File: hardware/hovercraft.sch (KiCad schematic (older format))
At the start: 40 parts, among them J1 USB_OTG, J10 CONN_01X02, J11 CONN_01X02, J12 CONN_01X02, J2 CONN_01X03, J3 CONN_01X03, J4 CONN_01X03, J5 CONN_01X03, J6 CONN_01X03, J7 CONN_01X03, J8 CONN_01X02, J9 CONN_01X02, SW1 RESET, SW2 BOOT, U1 HC-12, U2 ATMEGA32U2-AU, Y1 Crystal_GND24

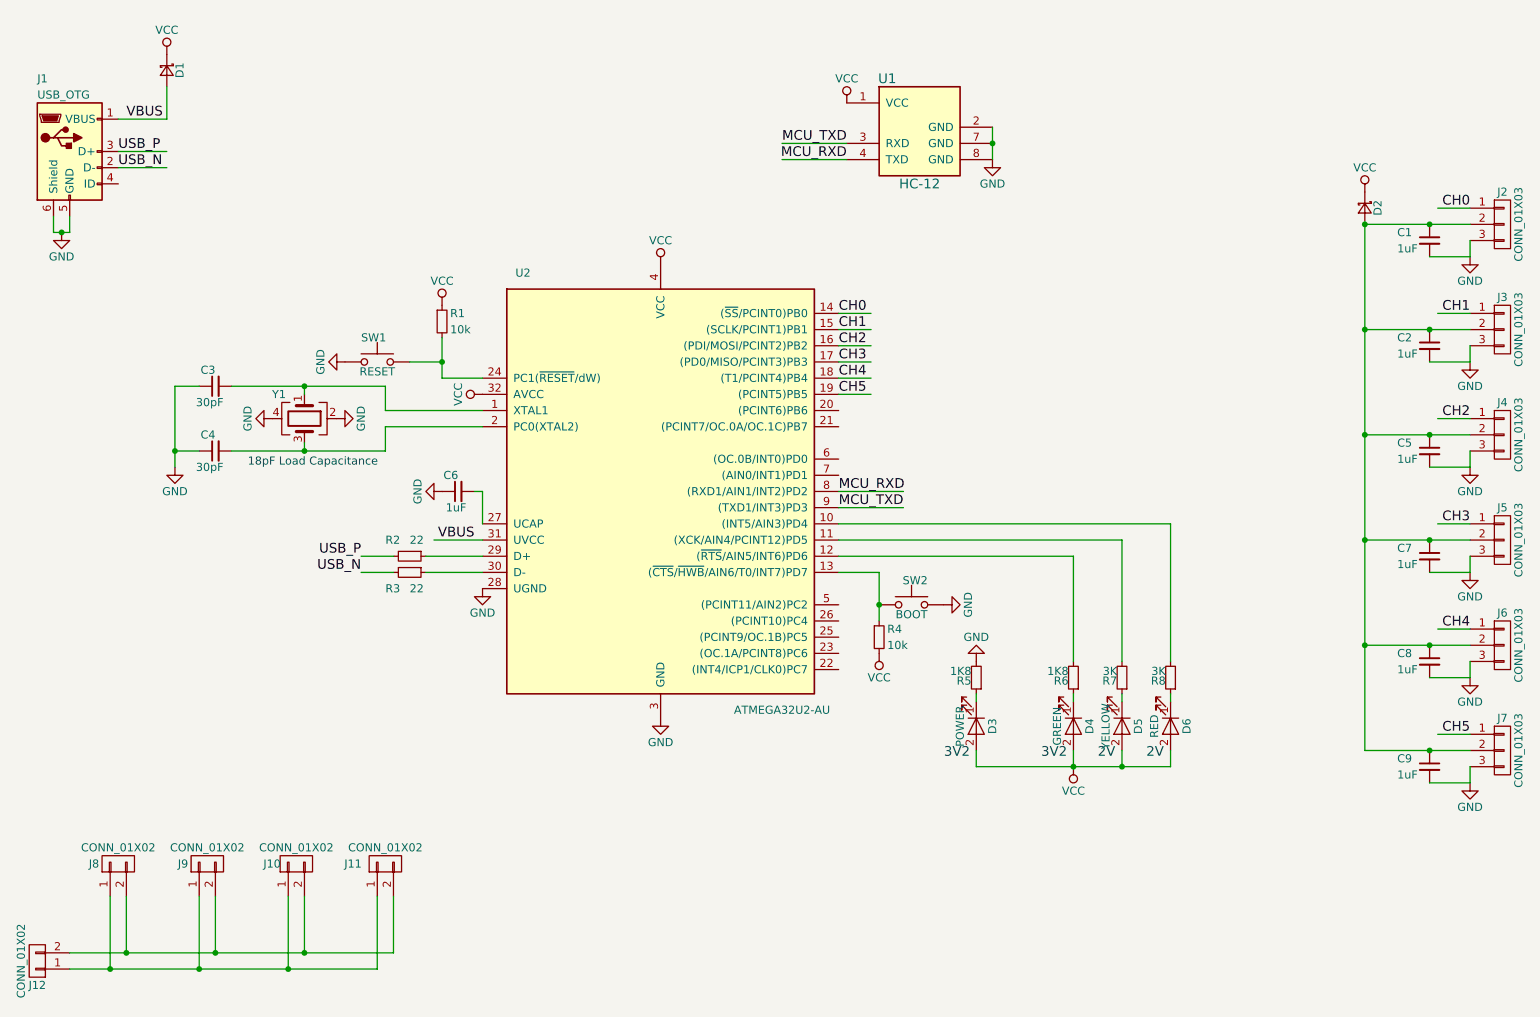
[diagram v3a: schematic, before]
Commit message: Moved the servo PWM signals to different pins to free up the SPI for a gyroscope/accelerometer/magnetometer
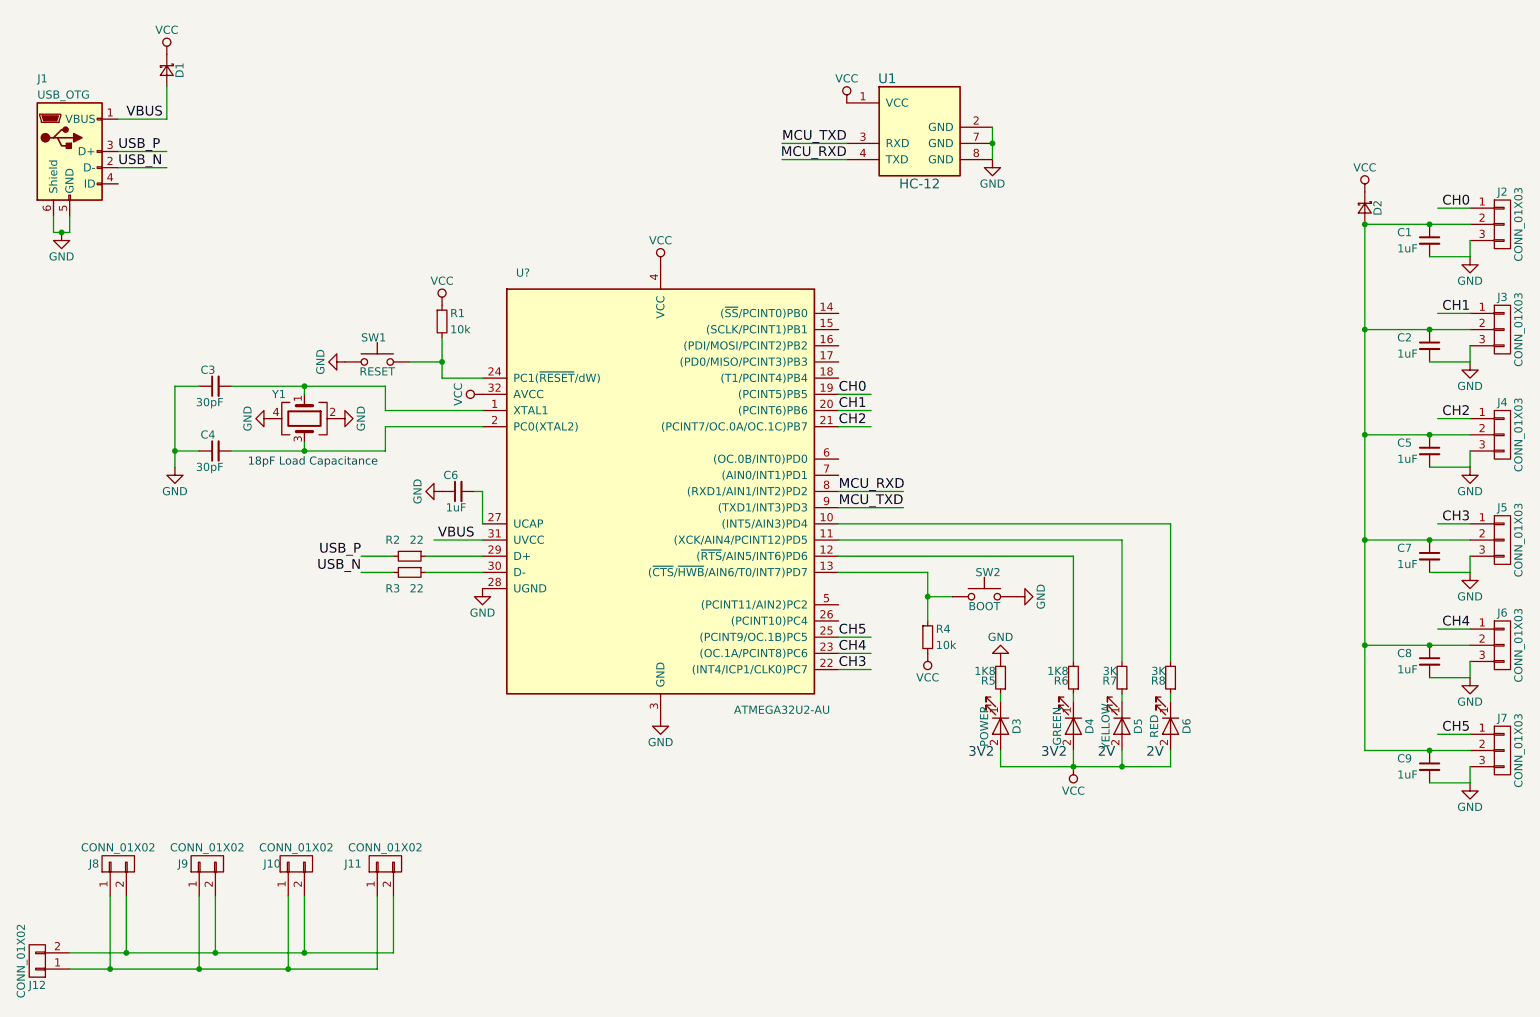
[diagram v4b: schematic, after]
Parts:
- removed U2: ATMEGA32U2-AU, Housings_DFN_QFN:QFN-32-1EP_5x5mm_Pitch0.5mm, symbol ATMEGA32U2-AU
- added U?: ATMEGA32U2-AU, TQFP-32, symbol ATMEGA32U2-AU
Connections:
- wire segments 91 -> 92
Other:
- moved on the sheet: D3, R4, R5, SW2
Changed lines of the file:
@@
-$EndComp
-$Comp
-L ATMEGA32U2-AU U2
-U 1 1 593A6E8E
-P 5200 3850
-F 0 "U2" H 4350 5200 50  0000 C CNN
-F 1 "ATMEGA32U2-AU" H 5950 2500 50  0000 C CNN
-F 2 "Housings_DFN_QFN:QFN-32-1EP_5x5mm_Pitch0.5mm" H 5050 3900 50  0001 C CNN
-F 3 "http://www.atmel.com/Images/doc7799.pdf" H 5300 2400 50  0001 C CNN
-	1    5200 3850
-	1    0    0    -1
 $EndComp
 $Comp
 L LED D3
 U 1 1 593B3BF4
-P 7150 5300
-F 0 "D3" H 7150 5400 50  0000 C CNN
-F 1 "POWER" H 7150 5200 50  0000 C CNN
-F 2 "LEDs:LED_0603" H 7150 5300 50  0001 C CNN
-F 3 "" H 7150 5300 50  0001 C CNN
-	1    7150 5300
+P 7300 5300
+F 0 "D3" H 7300 5400 50  0000 C CNN
+F 1 "POWER" H 7300 5200 50  0000 C CNN
+F 2 "LEDs:LED_0603" H 7300 5300 50  0001 C CNN
+F 3 "" H 7300 5300 50  0001 C CNN
+	1    7300 5300
 	0    1    1    0
 $EndComp
@@
 Text Notes 7550 5500 0    60   ~ 0
 3V2
-Text Notes 6950 5500 0    60   ~ 0
+Text Notes 7100 5500 0    60   ~ 0
 3V2
 $Comp
 L R_Small R5
 U 1 1 593B75C3
-P 7150 5000
-F 0 "R5" H 7180 5020 50  0000 L CNN
-F 1 "1K8" H 7180 4960 50  0000 L CNN
-F 2 "Resistors_SMD:R_0603" H 7150 5000 50  0001 C CNN
-F 3 "" H 7150 5000 50  0001 C CNN
-	1    7150 5000
+P 7300 5000
+F 0 "R5" H 7330 5020 50  0000 L CNN
+F 1 "1K8" H 7330 4960 50  0000 L CNN
+F 2 "Resistors_SMD:R_0603" H 7300 5000 50  0001 C CNN
+F 3 "" H 7300 5000 50  0001 C CNN
+	1    7300 5000
 	-1   0    0    1
 $EndComp
@@
 Text Label 10200 2100 2    60   ~ 0
 CH0
-Text Label 6300 3150 0    60   ~ 0
+Text Label 6300 4850 0    60   ~ 0
 CH4
-Text Label 6300 3050 0    60   ~ 0
+Text Label 6300 4950 0    60   ~ 0
 CH3
-Text Label 6300 2950 0    60   ~ 0
+Text Label 6300 3450 0    60   ~ 0
 CH2
-Text Label 6300 2850 0    60   ~ 0
+Text Label 6300 3350 0    60   ~ 0
 CH1
-Text Label 6300 2750 0    60   ~ 0
+Text Label 6300 3250 0    60   ~ 0
 CH0
 Text Label 4050 4150 2    60   ~ 0
@@
 L GND #PWR013
 U 1 1 593D7ED6
-P 7150 4900
-F 0 "#PWR013" H 7150 4650 50  0001 C CNN
-F 1 "GND" H 7150 4750 50  0000 C CNN
-F 2 "" H 7150 4900 50  0001 C CNN
-F 3 "" H 7150 4900 50  0001 C CNN
-	1    7150 4900
+P 7300 4900
+F 0 "#PWR013" H 7300 4650 50  0001 C CNN
+F 1 "GND" H 7300 4750 50  0000 C CNN
+F 2 "" H 7300 4900 50  0001 C CNN
+F 3 "" H 7300 4900 50  0001 C CNN
+	1    7300 4900
 	-1   0    0    1
 $EndComp
@@
 L SW_Push SW2
 U 1 1 593C198B
-P 6750 4550
-F 0 "SW2" H 6650 4700 50  0000 L CNN
-F 1 "BOOT" H 6750 4490 50  0000 C CNN
-F 2 "Buttons_Switches_SMD:Panasonic_EVQPUJ_EVQPUA" H 6750 4750 50  0001 C CNN
-F 3 "" H 6750 4750 50  0001 C CNN
-	1    6750 4550
+P 7200 4500
+F 0 "SW2" H 7100 4650 50  0000 L CNN
+F 1 "BOOT" H 7200 4440 50  0000 C CNN
+F 2 "Buttons_Switches_SMD:Panasonic_EVQPUJ_EVQPUA" H 7200 4700 50  0001 C CNN
+F 3 "" H 7200 4700 50  0001 C CNN
+	1    7200 4500
 	-1   0    0    -1
 $EndComp
@@
 L R_Small R4
 U 1 1 593C1F0C
-P 6550 4750
-F 0 "R4" H 6600 4800 50  0000 L CNN
-F 1 "10k" H 6600 4700 50  0000 L CNN
-F 2 "Resistors_SMD:R_0603" H 6550 4750 50  0001 C CNN
-F 3 "" H 6550 4750 50  0001 C CNN
-	1    6550 4750
+P 6850 4750
+F 0 "R4" H 6900 4800 50  0000 L CNN
+F 1 "10k" H 6900 4700 50  0000 L CNN
+F 2 "Resistors_SMD:R_0603" H 6850 4750 50  0001 C CNN
+F 3 "" H 6850 4750 50  0001 C CNN
+	1    6850 4750
 	1    0    0    -1
 $EndComp
@@
 L VCC #PWR016
 U 1 1 593C294F
-P 6550 4850
-F 0 "#PWR016" H 6550 4700 50  0001 C CNN
-F 1 "VCC" H 6550 5000 50  0000 C CNN
-F 2 "" H 6550 4850 50  0001 C CNN
-F 3 "" H 6550 4850 50  0001 C CNN
-	1    6550 4850
+P 6850 4850
+F 0 "#PWR016" H 6850 4700 50  0001 C CNN
+F 1 "VCC" H 6850 5000 50  0000 C CNN
+F 2 "" H 6850 4850 50  0001 C CNN
+F 3 "" H 6850 4850 50  0001 C CNN
+	1    6850 4850
 	-1   0    0    1
 $EndComp
@@
 L GND #PWR017
 U 1 1 593C2F8A
-P 6950 4550
-F 0 "#PWR017" H 6950 4300 50  0001 C CNN
-F 1 "GND" H 6950 4400 50  0000 C CNN
-F 2 "" H 6950 4550 50  0001 C CNN
-F 3 "" H 6950 4550 50  0001 C CNN
-	1    6950 4550
+P 7400 4500
+F 0 "#PWR017" H 7400 4250 50  0001 C CNN
+F 1 "GND" H 7400 4350 50  0000 C CNN
+F 2 "" H 7400 4500 50  0001 C CNN
+F 3 "" H 7400 4500 50  0001 C CNN
+	1    7400 4500
 	0    -1   -1   0
 $EndComp
@@
 Text Label 10200 5350 2    60   ~ 0
 CH5
-Text Label 6300 3250 0    60   ~ 0
+Text Label 6300 4750 0    60   ~ 0
 CH5
 $Comp
@@
 	3800 4150 4100 4150
 Wire Wire Line
-	7150 5150 7150 5100
+	7300 5150 7300 5100
 Wire Wire Line
 	7750 5150 7750 5100
@@
 	7750 5550 7750 5450
 Wire Wire Line
-	7150 5450 7150 5550
-Wire Wire Line
-	7150 5550 8350 5550
+	7300 5450 7300 5550
+Wire Wire Line
+	7300 5550 8350 5550
 Wire Wire Line
 	8350 5550 8350 5450
@@
 	3000 3550 3000 3600
 Wire Wire Line
-	6300 2750 6500 2750
-Wire Wire Line
-	6500 2850 6300 2850
-Wire Wire Line
-	6300 2950 6500 2950
-Wire Wire Line
-	6500 3050 6300 3050
-Wire Wire Line
-	6300 3150 6500 3150
-Wire Wire Line
 	10200 2100 10000 2100
 Wire Wire Line
@@
 Connection ~ 3850 3050
 Wire Wire Line
-	6550 4350 6550 4650
-Wire Wire Line
-	6300 4350 6550 4350
-Connection ~ 6550 4550
+	6300 4350 6850 4350
 Wire Wire Line
 	6350 1800 5950 1800
@@
 	6500 3250 6300 3250
 Wire Wire Line
-	9550 5450 9550 2200
+	9550 2200 9550 5450
 Wire Wire Line
 	7250 1600 7250 1800
@@
 Connection ~ 9550 4800
 Connection ~ 9550 2200
+Wire Wire Line
+	7000 4500 6850 4500
+Wire Wire Line
+	6850 4350 6850 4650
+Connection ~ 6850 4500
+Wire Wire Line
+	6300 3350 6500 3350
+Wire Wire Line
+	6500 3450 6300 3450
+Wire Wire Line
+	6300 4750 6500 4750
+Wire Wire Line
+	6300 4850 6500 4850
+Wire Wire Line
+	6300 4950 6500 4950
+$Comp
+L ATMEGA32U2-AU U?
+U 1 1 593FB614
+P 5200 3850
+F 0 "U?" H 4350 5200 50  0000 C CNN
+F 1 "ATMEGA32U2-AU" H 5950 2500 50  0000 C CNN
+F 2 "TQFP-32" H 5050 3900 50  0001 C CNN
+F 3 "http://www.atmel.com/Images/doc7799.pdf" H 5300 2400 50  0001 C CNN
+	1    5200 3850
+	1    0    0    -1
+$EndComp
 $EndSCHEMATC
